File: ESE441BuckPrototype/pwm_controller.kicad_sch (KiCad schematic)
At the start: 22 parts

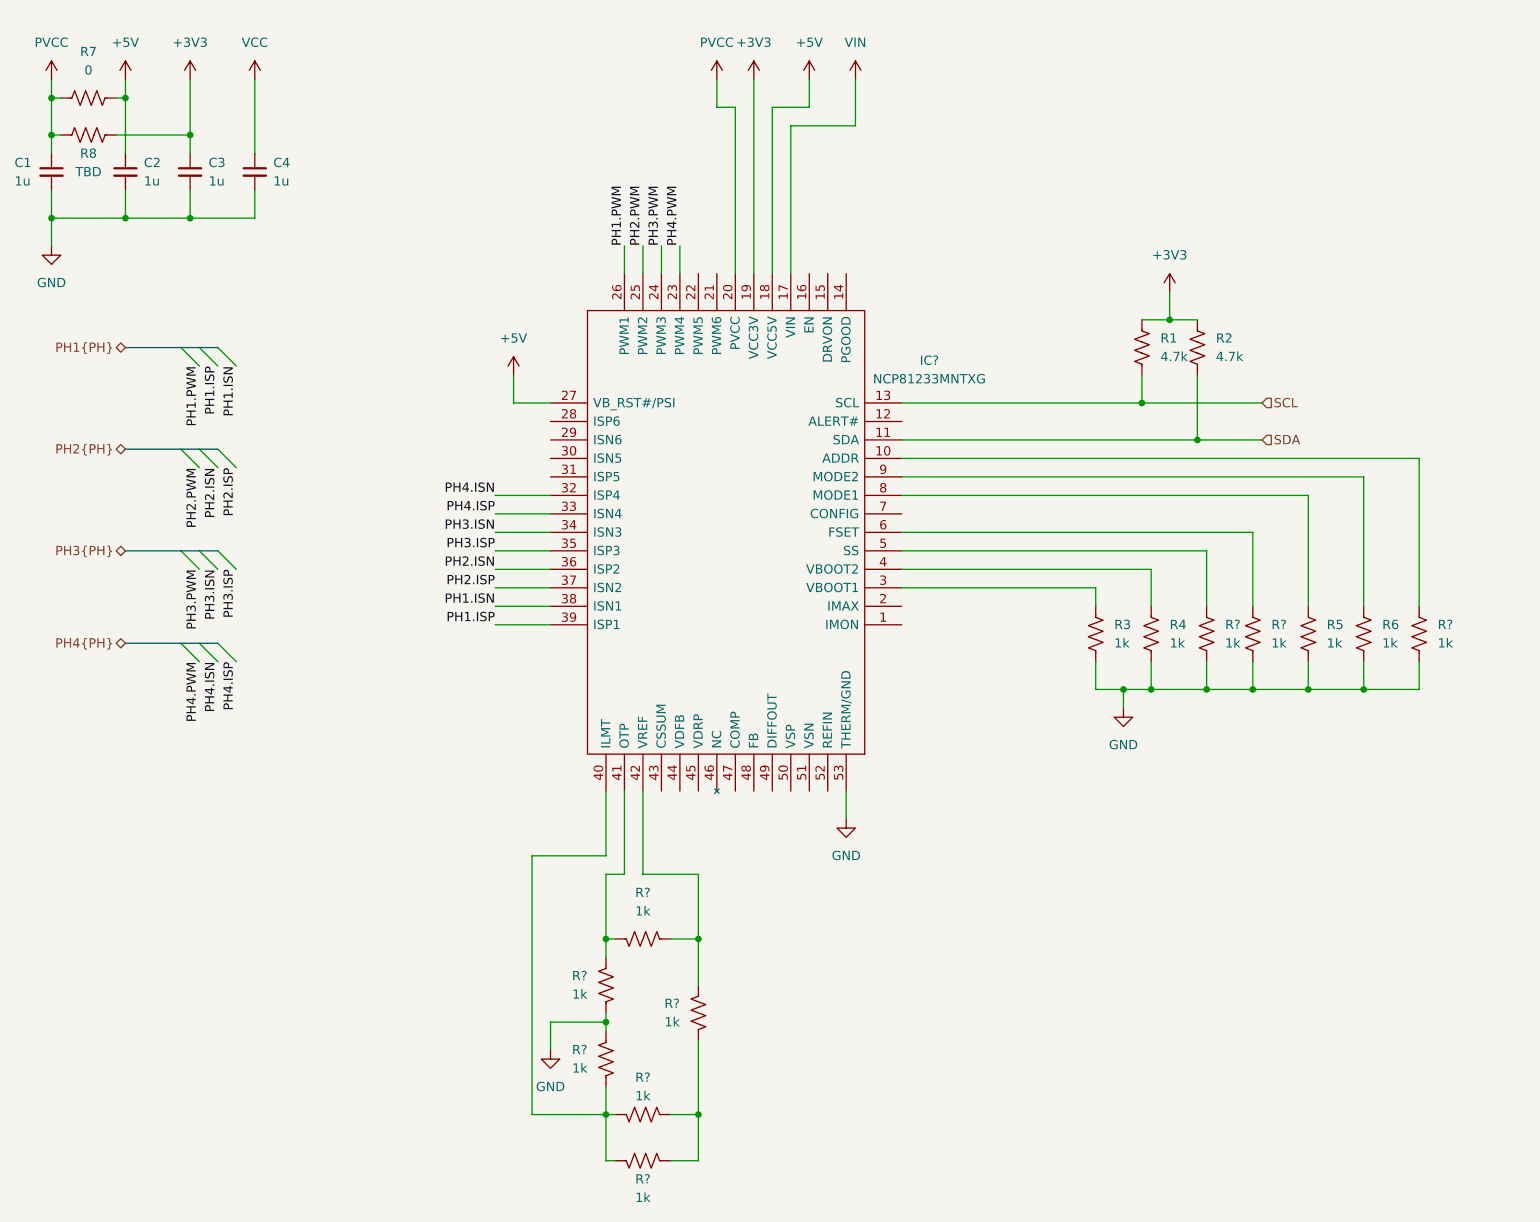
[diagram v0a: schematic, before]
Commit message: Change setting resistor values
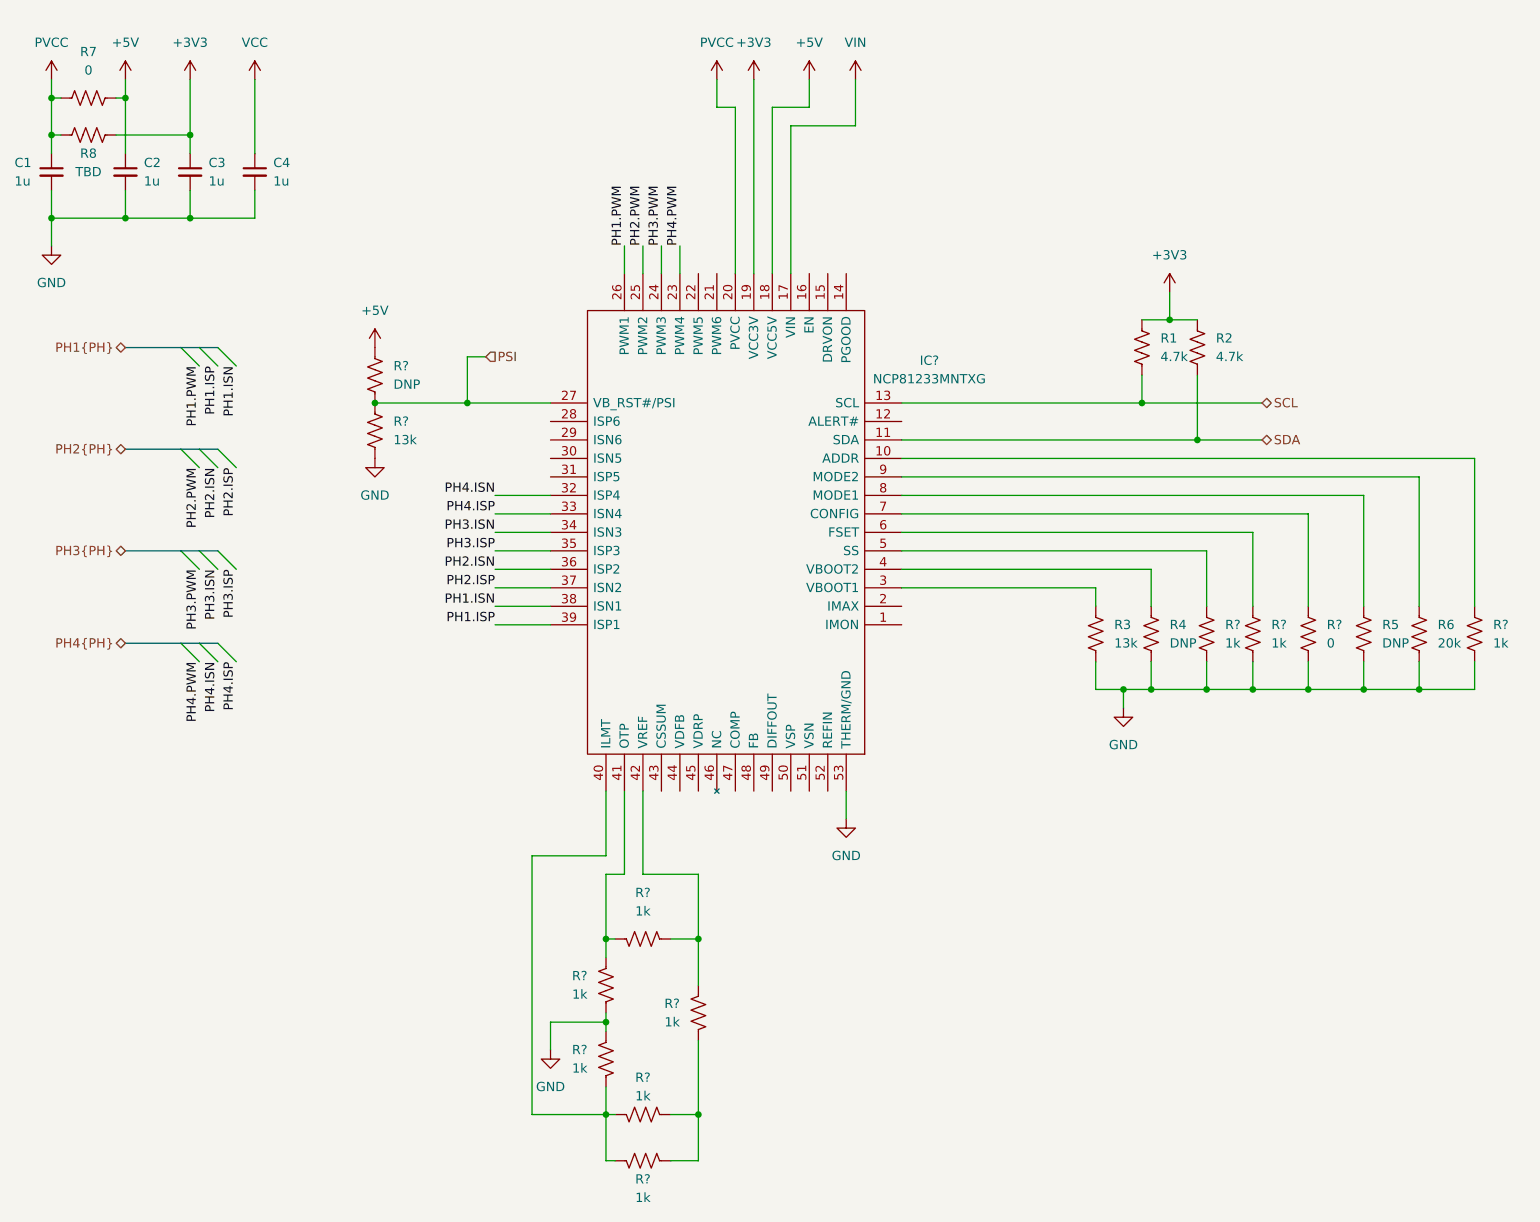
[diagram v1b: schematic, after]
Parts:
- added R?: 13k, Resistor_SMD:R_0603_1608Metric, symbol Device:R_US
- added R?: DNP, Resistor_SMD:R_0603_1608Metric, symbol Device:R_US
- added R?: 0, Resistor_SMD:R_0603_1608Metric, symbol Device:R_US
- R3: value 1k -> 13k
- R4, R5: value 1k -> DNP
- R6: value 1k -> 20k
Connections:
- net +5V: now also R?.1; no longer IC?.27 (VB_RST#/PSI)
- net GND: now also R?.2, R?.2
- net at IC?.7 (CONFIG): now also R?.1
- new net PSI: IC?.27 (VB_RST#/PSI), R?.1, R?.2
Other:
- moved on the sheet: R5, R6, R?

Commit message: Add feedback network
Todo: set proper values and implement current monitoring
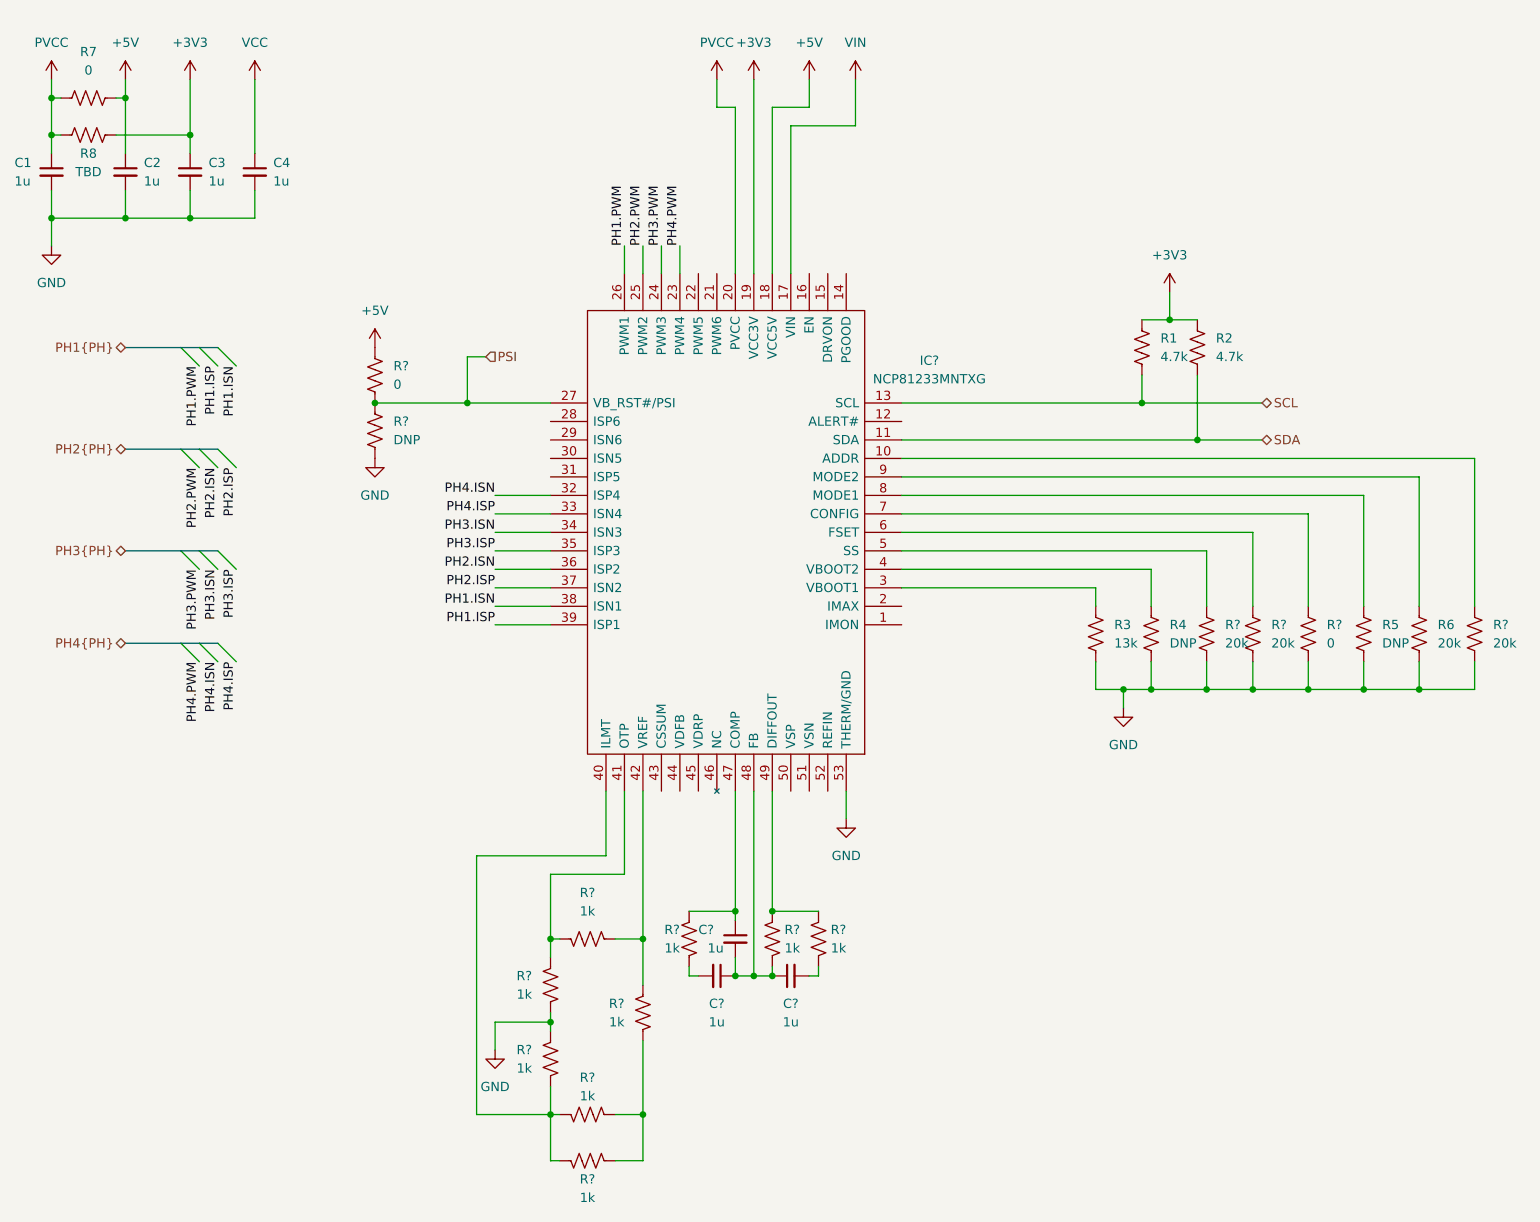
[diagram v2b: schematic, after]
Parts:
- added C? (x3): 1u, symbol Device:C_Small
- added R? (x3): 1k, Resistor_SMD:R_0603_1608Metric, symbol Device:R_US
- R?: value 13k -> DNP
- R?: value DNP -> 0
- R? (x3): value 1k -> 20k
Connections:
- net at IC?.47 (COMP): now also C?.1, R?.1
- net at IC?.48 (FB): now also C?.1, C?.1, C?.2, R?.2
- net at IC?.49 (DIFFOUT): now also R?.1, R?.1
- new net: C?.2, R?.2 (x2)
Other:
- moved on the sheet: R?

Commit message: Change R8 to do not place
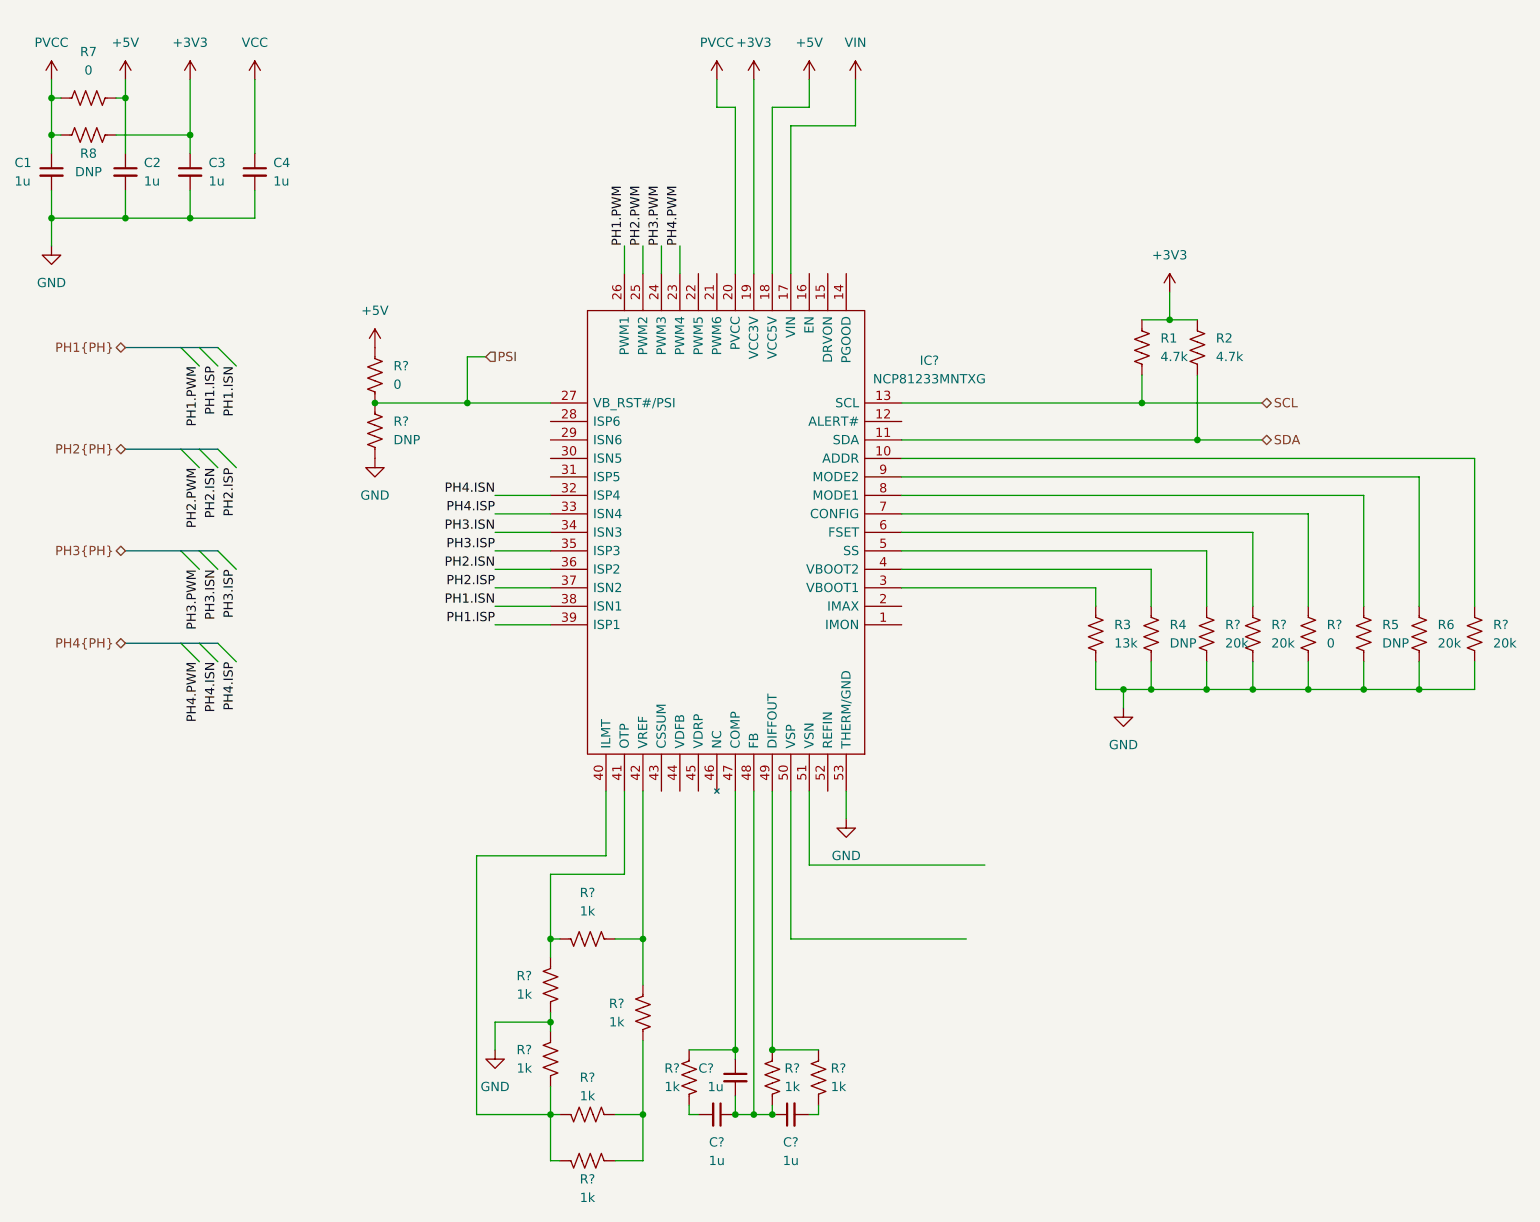
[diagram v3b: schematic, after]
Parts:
- R8: value TBD -> DNP
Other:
- moved on the sheet: C?, R?

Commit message: Add output voltage sensing, Imax/Imon
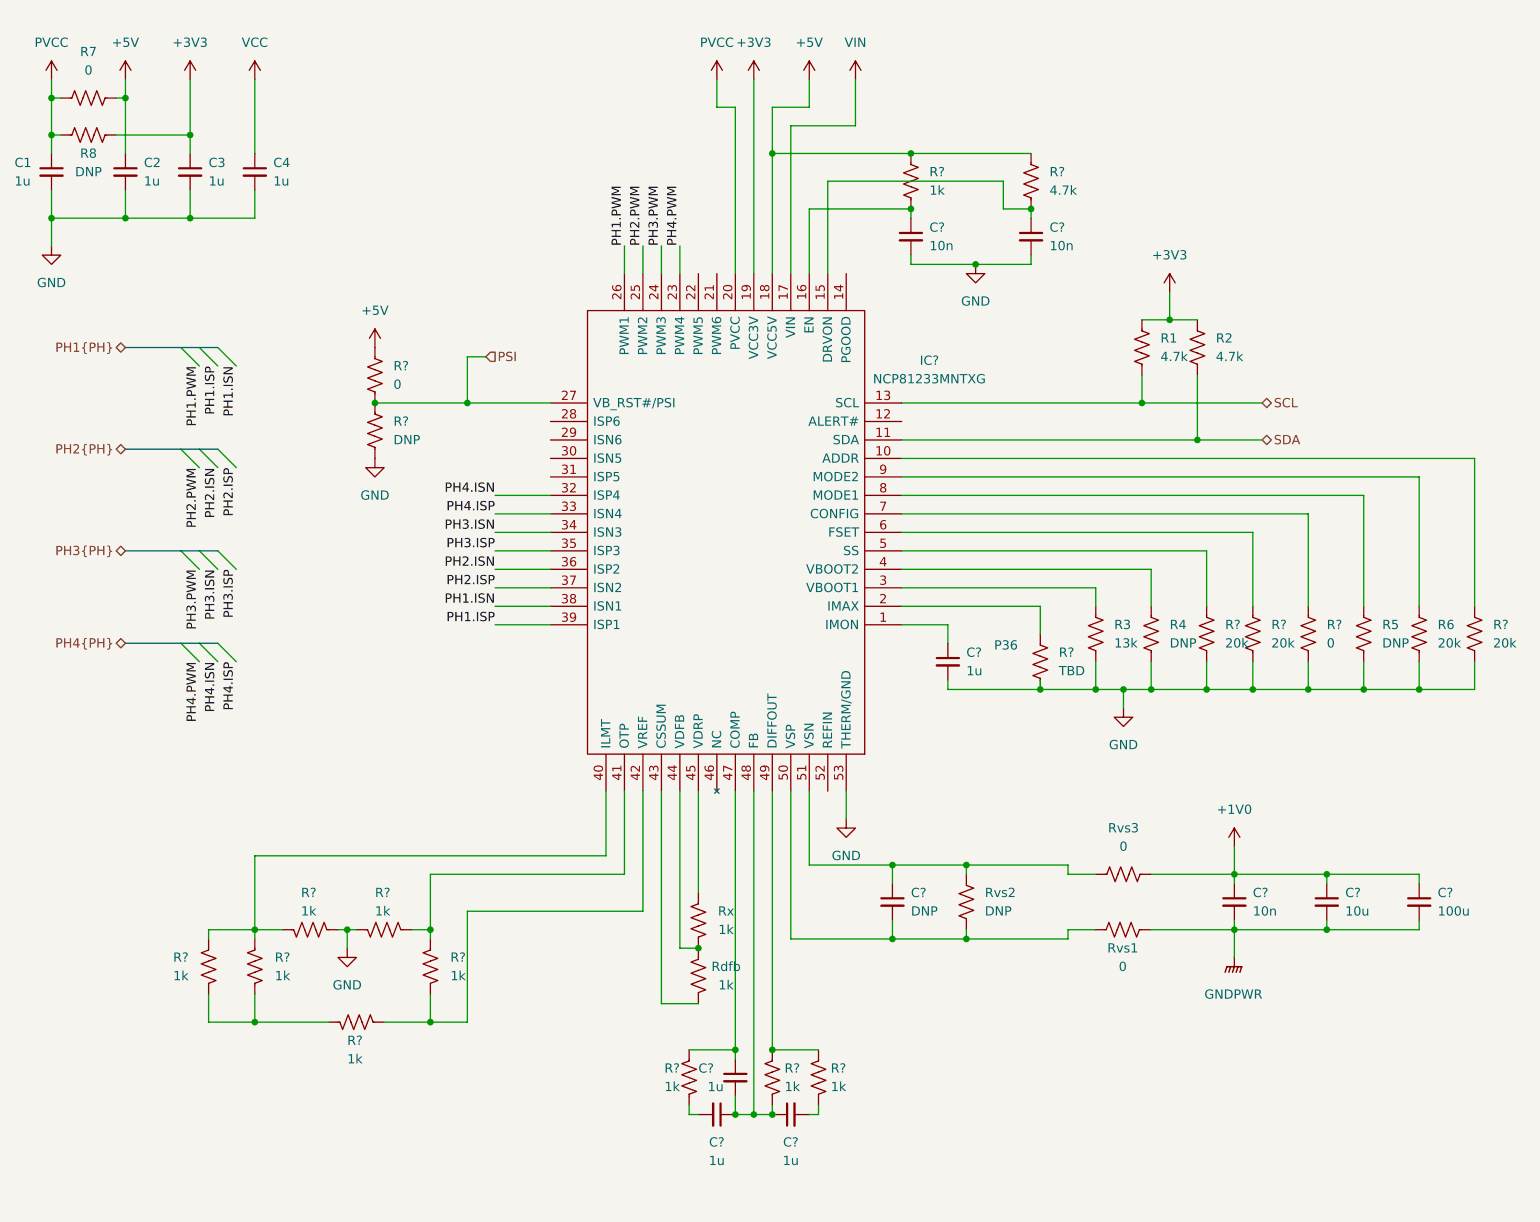
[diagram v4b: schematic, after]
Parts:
- added C?: 1u, symbol Device:C_Small
- added C? (x3): 10n, symbol Device:C_Small
- added C?: 100u, symbol Device:C_Small
- added C?: DNP, symbol Device:C_Small
- added C?: 10u, symbol Device:C_Small
- added R?: 4.7k, Resistor_SMD:R_0603_1608Metric, symbol Device:R_US
- added R?: TBD, Resistor_SMD:R_0603_1608Metric, symbol Device:R_US
- added R?, Rdfb, Rx: 1k, Resistor_SMD:R_0603_1608Metric, symbol Device:R_US
- added Rvs1, Rvs3: 0, Resistor_SMD:R_0603_1608Metric, symbol Device:R_US
- added Rvs2: DNP, Resistor_SMD:R_0603_1608Metric, symbol Device:R_US
- R4: footprint (none) -> Resistor_SMD:R_0603_1608Metric
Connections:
- net +5V: now also R?.1, R?.1
- net GND: now also C?.2, C?.2, C?.2, R?.2
- net at IC?.1 (IMON): now also C?.1
- net at IC?.15 (DRVON): now also C?.1, R?.2
- net at IC?.16 (EN): now also C?.1, R?.2
- net at IC?.2 (IMAX): now also R?.1
- net at IC?.43 (CSSUM): now also Rdfb.1
- net at IC?.44 (VDFB): now also Rdfb.2, Rx.1
- net at IC?.45 (VDRP): now also Rx.2
- net at IC?.50 (VSP): now also C?.2, Rvs1.1, Rvs2.2
- net at IC?.51 (VSN): now also C?.1, Rvs2.1, Rvs3.1
- new net +1V0: C?.1, C?.1, C?.1, Rvs3.2
- new net GNDPWR: C?.2, C?.2, C?.2, Rvs1.2
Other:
- note added: "P36"
- moved on the sheet: R?
